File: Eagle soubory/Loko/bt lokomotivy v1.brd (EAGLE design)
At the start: 40.2 x 18 mm, 24 parts, among them IC1 MEGA8-AI, IC2 HT7533-1 TO92, IC6 L6470, Q2 16MHz, U1 HC_05

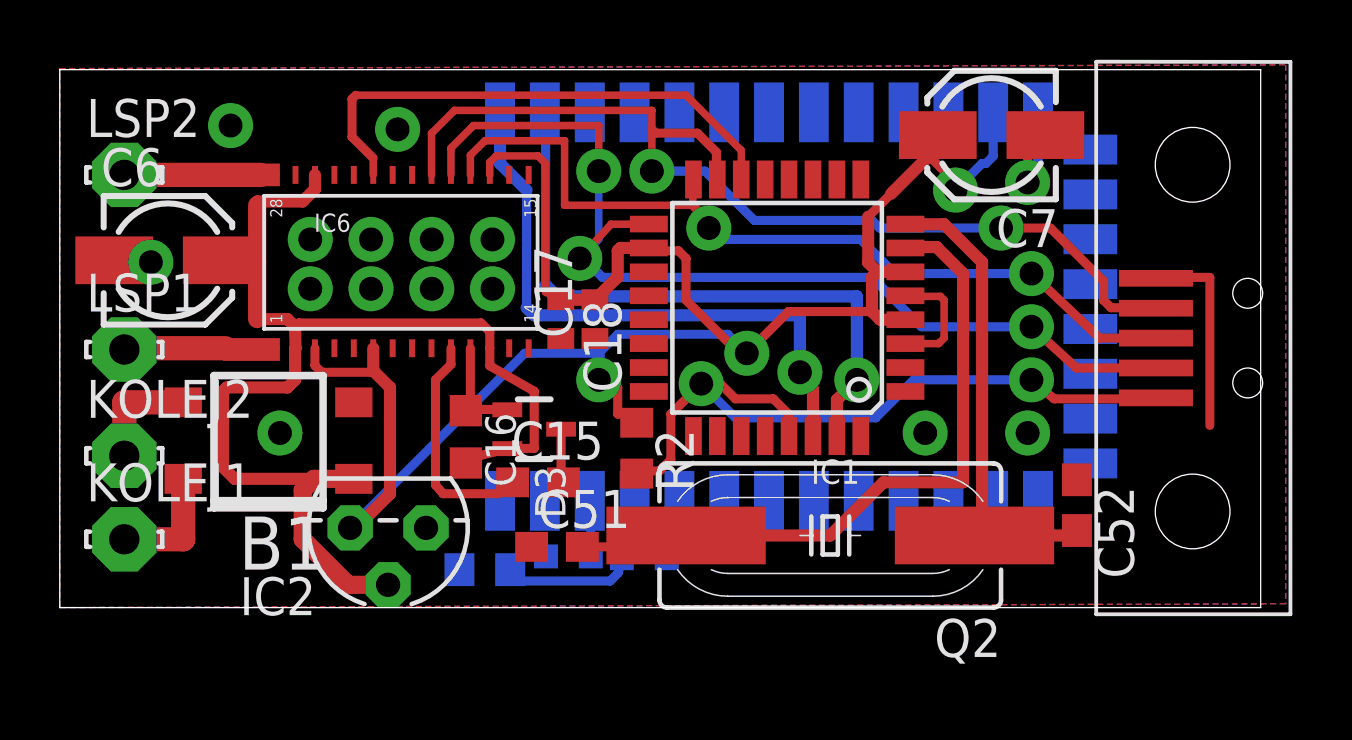
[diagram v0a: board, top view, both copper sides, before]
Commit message: added servopřestavník
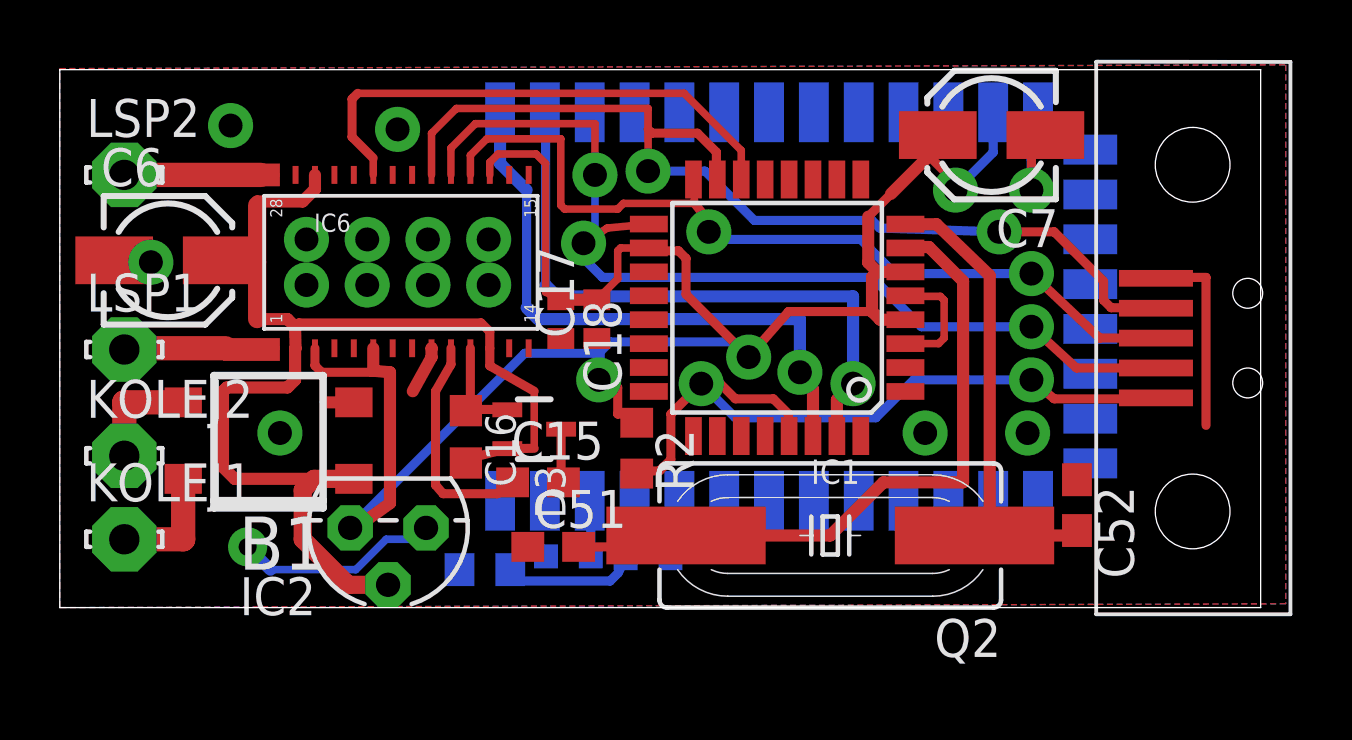
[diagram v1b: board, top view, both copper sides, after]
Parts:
- moved C51 0.13 mm to (16.5, 2.03)
- moved LED1 0.13 mm to (19.7, 1.65)
- moved C17 0.06 mm to (18.0, 9.65)
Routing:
- net GND: track 13.8 -> 23.8 mm, vias 15 -> 16
- net SCK: track 34.4 -> 33.7 mm
